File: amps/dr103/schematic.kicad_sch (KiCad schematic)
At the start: 97 parts, among them T1 OT

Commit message: Fix: schematic sheets — real title block, fitted paper, no lettering through circuitry
Every sheet in the corpus shipped with an EMPTY title block ("Title:" and
"Date:" blank, default "Sheet /" furniture) laid onto a fixed A4/A3 page
regardless of the drawing's size, with prose annotations placed by hand
wherever a coordinate looked free when the amp was first drawn. The result
read as an unfinished alpha under a `verified` badge: KiCanvas's default view
is `zoom_to_page()`, so a 150 x 110 mm circuit on an A3 sheet opened as a
postage stamp, and later edits had pushed live circuitry under the prose.

schematic_lib.py — the builder now records each element as a (kind, points,
extra) tuple instead of a finished string, so `write()` can measure and move
what it emits:

- emits a real `(title_block …)` read from the amp's own meta.yaml — Title =
  designation + style, Date = the verification (or added) date, Rev = the
  verification status, Company = Circuit Codex, plus the licence and source
  URL as comments. Fixes all 34 sheets from one place;
- emits `(paper "User" w h)` cut to the drawing, translated to a fixed margin,
  with the bottom 34 mm strip reserved for the worksheet's title block. Sheet
  utilisation of the drawable area went from as low as ~20% to 92-98%;
- `note()` queues prose into a wrapped band under the circuit, and `caption()`
  places a section heading over the block it names, nudging it clear if it
  would print through anything;
- per-symbol default label offsets (the old single default printed every pot's
  value through its own wiper arrow and every transformer's designator through
  its body), plus `place_labels()`, which moves any designator/value block that
  would print over ink;
- transformers and chokes are drawn, not boxed: iron core between two windings,
  centre taps where the part has them, and an optional `spec` lettering slot for
  a ratio or impedance;
- `gnd()` takes a direction, because a flag defaulting to "down" at the HEAD of
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
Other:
- note removed: "DR103 — Hiwatt Custom 100-style · Circuit Codex · CC-BY-SA 4.0 · redrawn from circuit facts"
- company: (none) -> Circuit Codex
- title: (none) -> DR103 — Hiwatt Custom 100-style

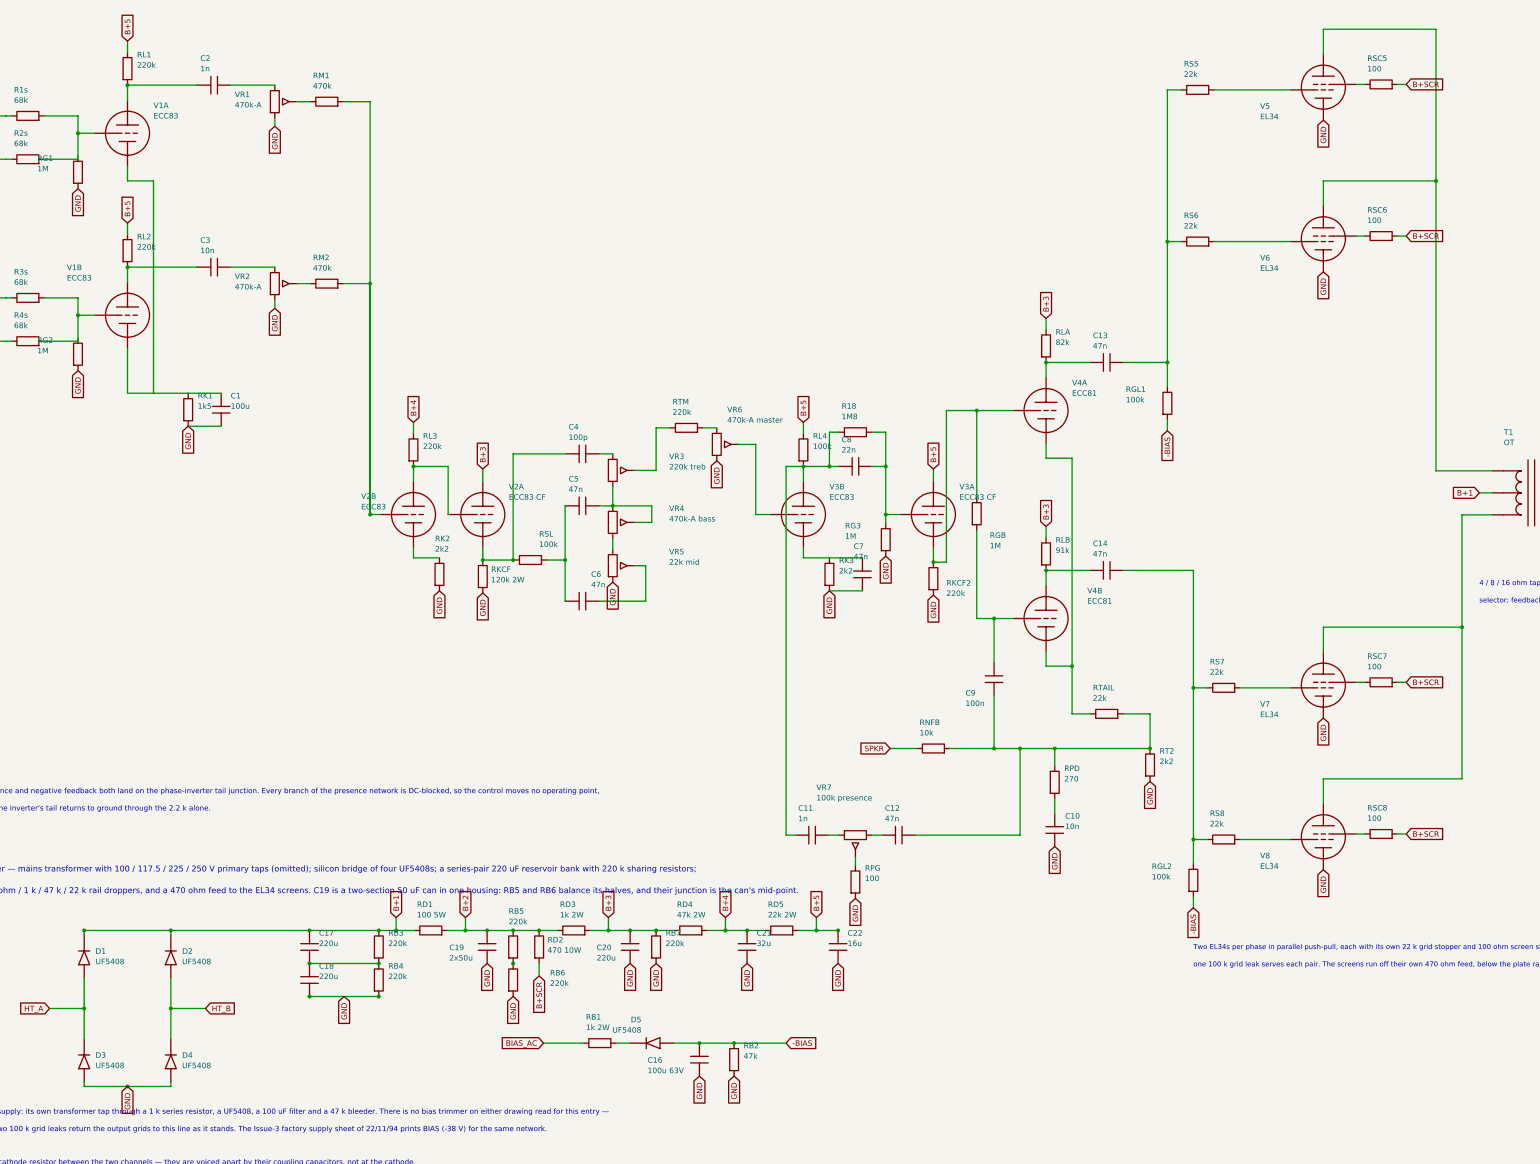
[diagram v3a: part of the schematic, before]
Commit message: Fix: deterministic schematic ids and wires split at every join
- _u() is uuid5 over (amp id, emission order), so a regeneration of an
  unchanged script is byte-identical and a drift gate becomes possible
- write() splits wire segments at symbol pins, wire ends and junction dots,
  so the file connects exactly what the drawing shows under KiCad's
  endpoint-only semantics (270 pins were on a wire's interior; net
  partitions unchanged on all 38 sheets)
- all sheets regenerated; aa864-bassman title block was stale (draft) and
  now matches meta.yaml (verified)

Co-Authored-By: Claude Fable 5.1 <noreply@anthropic.com>
Claude-Session: https://claude.ai/code/session_01KBMfdh37HmCL2iWcBiL5J1
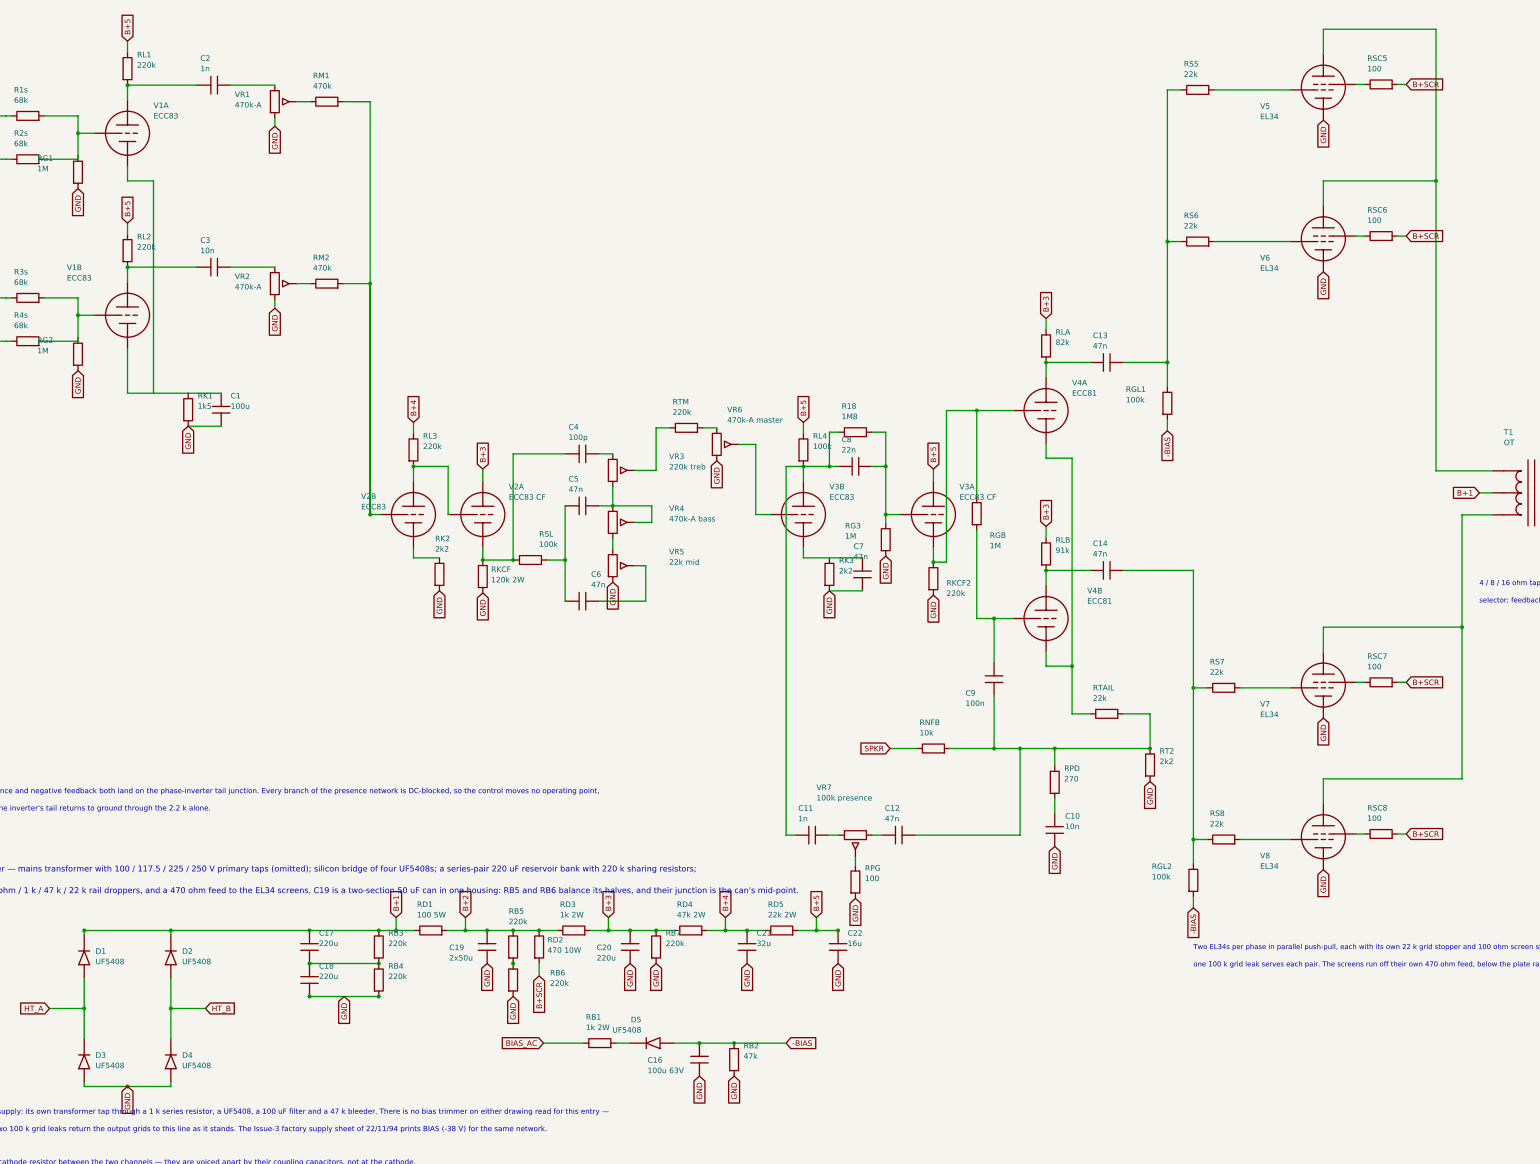
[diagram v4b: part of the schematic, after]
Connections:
- net at R1s.2, R2s.2, V1A.2 (G): now also RG1.1
- net at RG2.1: now also R3s.2, R4s.2, V1B.2 (G)
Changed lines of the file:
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@@
   (wire (pts (xy 36.146 44.278) (xy 43.906 44.278))
     (stroke (width 0) (type default)))
-  (wire (pts (xy 43.906 44.278) (xy 43.906 38.278))
+  (wire (pts (xy 43.906 44.278) (xy 43.906 43.468))
+    (stroke (width 0) (type default)))
+  (wire (pts (xy 43.906 43.468) (xy 43.906 38.278))
     (stroke (width 0) (type default)))
   (junction (at 43.906 38.278) (diameter 0) (color 0 0 0 0))
@@
   (wire (pts (xy 105.146 30.988) (xy 111.336 30.988))
     (stroke (width 0) (type default)))
-  (wire (pts (xy 111.336 30.988) (xy 111.336 126.278))
+  (wire (pts (xy 111.336 30.988) (xy 111.336 72.988))
+    (stroke (width 0) (type default)))
+  (wire (pts (xy 111.336 72.988) (xy 111.336 126.278))
     (stroke (width 0) (type default)))
   (symbol (lib_id "cx:TRIODE") (at 55.336 80.278 0) (unit 1)
@@
   (wire (pts (xy 36.146 86.278) (xy 43.906 86.278))
     (stroke (width 0) (type default)))
-  (wire (pts (xy 43.906 86.278) (xy 43.906 80.278))
+  (wire (pts (xy 43.906 86.278) (xy 43.906 85.468))
+    (stroke (width 0) (type default)))
+  (wire (pts (xy 43.906 85.468) (xy 43.906 80.278))
     (stroke (width 0) (type default)))
   (junction (at 43.906 80.278) (diameter 0) (color 0 0 0 0))
@@
   (wire (pts (xy 244.336 137.278) (xy 244.336 102.278))
     (stroke (width 0) (type default)))
-  (wire (pts (xy 244.336 102.278) (xy 259.716 102.278))
+  (wire (pts (xy 244.336 102.278) (xy 251.336 102.278))
+    (stroke (width 0) (type default)))
+  (wire (pts (xy 251.336 102.278) (xy 259.716 102.278))
     (stroke (width 0) (type default)))
   (junction (at 251.336 102.278) (diameter 0) (color 0 0 0 0))
@@
   (wire (pts (xy 251.336 129.898) (xy 251.336 150.278))
     (stroke (width 0) (type default)))
-  (wire (pts (xy 251.336 150.278) (xy 259.716 150.278))
+  (wire (pts (xy 251.336 150.278) (xy 255.336 150.278))
+    (stroke (width 0) (type default)))
+  (wire (pts (xy 255.336 150.278) (xy 259.716 150.278))
     (stroke (width 0) (type default)))
   (wire (pts (xy 267.336 94.658) (xy 267.336 91.178))
@@
   (wire (pts (xy 267.336 161.278) (xy 273.336 161.278))
     (stroke (width 0) (type default)))
-  (wire (pts (xy 273.336 113.278) (xy 273.336 172.278))
+  (wire (pts (xy 273.336 113.278) (xy 273.336 161.278))
+    (stroke (width 0) (type default)))
+  (wire (pts (xy 273.336 161.278) (xy 273.336 172.278))
     (stroke (width 0) (type default)))
   (junction (at 273.336 161.278) (diameter 0) (color 0 0 0 0))
@@
   (global_label "SPKR" (shape input) (at 231.336 180.278 180)
     (effects (font (size 1.27 1.27)) (justify right)))
-  (wire (pts (xy 255.336 180.278) (xy 291.336 180.278))
+  (wire (pts (xy 255.336 180.278) (xy 261.336 180.278))
+    (stroke (width 0) (type default)))
+  (wire (pts (xy 261.336 180.278) (xy 269.336 180.278))
+    (stroke (width 0) (type default)))
+  (wire (pts (xy 269.336 180.278) (xy 291.336 180.278))
     (stroke (width 0) (type default)))
   (junction (at 269.336 180.278) (diameter 0) (color 0 0 0 0))
@@
   (wire (pts (xy 285.146 91.178) (xy 295.336 91.178))
     (stroke (width 0) (type default)))
-  (wire (pts (xy 295.336 28.278) (xy 295.336 91.178))
+  (wire (pts (xy 295.336 28.278) (xy 295.336 63.278))
+    (stroke (width 0) (type default)))
+  (wire (pts (xy 295.336 63.278) (xy 295.336 91.178))
     (stroke (width 0) (type default)))
   (junction (at 295.336 63.278) (diameter 0) (color 0 0 0 0))
@@
   (wire (pts (xy 285.146 139.178) (xy 301.336 139.178))
     (stroke (width 0) (type default)))
-  (wire (pts (xy 301.336 139.178) (xy 301.336 201.278))
+  (wire (pts (xy 301.336 139.178) (xy 301.336 166.278))
+    (stroke (width 0) (type default)))
+  (wire (pts (xy 301.336 166.278) (xy 301.336 201.278))
     (stroke (width 0) (type default)))
   (junction (at 301.336 166.278) (diameter 0) (color 0 0 0 0))
@@
   (wire (pts (xy 331.336 14.278) (xy 357.336 14.278))
     (stroke (width 0) (type default)))
-  (wire (pts (xy 357.336 14.278) (xy 357.336 116.198))
+  (wire (pts (xy 357.336 14.278) (xy 357.336 49.278))
+    (stroke (width 0) (type default)))
+  (wire (pts (xy 357.336 49.278) (xy 357.336 116.198))
     (stroke (width 0) (type default)))
   (wire (pts (xy 331.336 55.023) (xy 331.336 49.278))
@@
   (wire (pts (xy 331.336 187.278) (xy 363.336 187.278))
     (stroke (width 0) (type default)))
-  (wire (pts (xy 363.336 187.278) (xy 363.336 126.358))
+  (wire (pts (xy 363.336 187.278) (xy 363.336 152.278))
+    (stroke (width 0) (type default)))
+  (wire (pts (xy 363.336 152.278) (xy 363.336 126.358))
     (stroke (width 0) (type default)))
   (junction (at 363.336 152.278) (diameter 0) (color 0 0 0 0))
@@
   (wire (pts (xy 45.336 222.278) (xy 65.336 222.278))
     (stroke (width 0) (type default)))
-  (wire (pts (xy 45.336 258.278) (xy 65.336 258.278))
+  (wire (pts (xy 45.336 258.278) (xy 55.336 258.278))
+    (stroke (width 0) (type default)))
+  (wire (pts (xy 55.336 258.278) (xy 65.336 258.278))
     (stroke (width 0) (type default)))
   (global_label "GND" (shape input) (at 55.336 258.278 270)
     (effects (font (size 1.27 1.27)) (justify right)))
   (junction (at 55.336 258.278) (diameter 0) (color 0 0 0 0))
-  (wire (pts (xy 65.336 222.278) (xy 117.336 222.278))
+  (wire (pts (xy 65.336 222.278) (xy 97.336 222.278))
+    (stroke (width 0) (type default)))
+  (wire (pts (xy 97.336 222.278) (xy 113.336 222.278))
+    (stroke (width 0) (type default)))
+  (wire (pts (xy 113.336 222.278) (xy 117.336 222.278))
     (stroke (width 0) (type default)))
   (symbol (lib_id "cx:C") (at 97.336 226.088 0) (unit 1)
@@
   (global_label "GND" (shape input) (at 138.336 229.898 270)
     (effects (font (size 1.27 1.27)) (justify right)))
-  (wire (pts (xy 133.336 222.278) (xy 150.336 222.278))
+  (wire (pts (xy 133.336 222.278) (xy 138.336 222.278))
+    (stroke (width 0) (type default)))
+  (wire (pts (xy 138.336 222.278) (xy 144.336 222.278))
+    (stroke (width 0) (type default)))
+  (wire (pts (xy 144.336 222.278) (xy 150.336 222.278))
     (stroke (width 0) (type default)))
   (junction (at 144.336 222.278) (diameter 0) (color 0 0 0 0))
@@
   (global_label "GND" (shape input) (at 177.336 229.898 270)
     (effects (font (size 1.27 1.27)) (justify right)))
-  (wire (pts (xy 166.336 222.278) (xy 181.526 222.278))
+  (wire (pts (xy 166.336 222.278) (xy 171.336 222.278))
+    (stroke (width 0) (type default)))
+  (wire (pts (xy 171.336 222.278) (xy 177.336 222.278))
+    (stroke (width 0) (type default)))
+  (wire (pts (xy 177.336 222.278) (xy 181.526 222.278))
     (stroke (width 0) (type default)))
   (symbol (lib_id "cx:R") (at 185.336 222.278 90) (unit 1)
@@
   (global_label "GND" (shape input) (at 198.336 229.898 270)
     (effects (font (size 1.27 1.27)) (justify right)))
-  (wire (pts (xy 193.336 222.278) (xy 202.526 222.278))
+  (wire (pts (xy 193.336 222.278) (xy 198.336 222.278))
+    (stroke (width 0) (type default)))
+  (wire (pts (xy 198.336 222.278) (xy 202.526 222.278))
     (stroke (width 0) (type default)))
   (symbol (lib_id "cx:R") (at 206.336 222.278 90) (unit 1)
@@
     (property "Reference" "RD5" (at 203.136 216.278 270) (effects (font (size 1.27 1.27)) (justify left)))
     (property "Value" "22k 2W" (at 203.136 218.678 270) (effects (font (size 1.27 1.27)) (justify left))))
-  (wire (pts (xy 210.146 222.278) (xy 219.336 222.278))
+  (wire (pts (xy 210.146 222.278) (xy 214.336 222.278))
+    (stroke (width 0) (type default)))
+  (wire (pts (xy 214.336 222.278) (xy 219.336 222.278))
     (stroke (width 0) (type default)))
   (junction (at 214.336 222.278) (diameter 0) (color 0 0 0 0))

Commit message: Add: real tube pin numbers and readable valve glyphs on every schematic
Phase B of the drawing program. A factory service sheet numbers every tube
pin, because the number is what a technician puts a probe on. This corpus
printed none, and the numbers hidden in its symbols were positional
placeholders (P=1, G=2, K=3) that would have published a 6V6GT's plate as
pin 1 when it is pin 3.

1055 electrodes now carry the real number, 1027 lettered (27 are shared
filaments deduped, 1 dropped for want of clear space on the 6G2). Resolved per
instance from reference/tubes/<slug>.yaml through the same alias resolution the
layout renderer uses, so a 12AX7 section and a 6SL7 section each get their own
basing. A valve whose basing the corpus does not carry prints nothing rather
than a wrong number.

Section letters and basing units are now separate things, which cost a detour
worth recording. The RCA 12AX7-A sheet reads "Pin 1 - Plate of Unit No.2 ...
Pin 6 - Plate of Unit No.1", so unit numbering is not pin order; the 5Y3 and
GZ34 number their units in opposite pin order, so nothing positional can
express it. But the section LETTER is a designator, not a basing fact: this
corpus, like every technician, calls the first stage in signal order V1A, and
five amps' prose already did. On four amps the factory sheets put that first
stage on the other half -- the AA764's own schematic prints +200 V on pin 1 --
so those drawings now state their unit explicitly, each citing its source, and
no letter, netlist, parts list or layout comment changed. 183 layout comments
agree with the printed numbers, 0 disagree. A guard fires if two halves of one
bottle resolve to the same unit, which is exactly how this was found.

Glyphs: the cathode gains a bracket and filament hairpin so it can no longer be
confused with the plate bar, the pentode's screen sits on its own row, and a
rectifier draws as one envelope over its sections instead of two apparent
bottles. Line weights are scaled per sheet to a co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
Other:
- note added: "1"
- note added: "2"
- note added: "3"
- note added: "4"
- note added: "5"
- note added: "6"
- note added: "7"
- note added: "8"
